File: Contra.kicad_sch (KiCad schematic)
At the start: 10 parts, among them J1 Conn_01x03, J2 Conn_01x02, SW1 SW_PUSH, SW2 SW_SPDT, U1 ProMicro

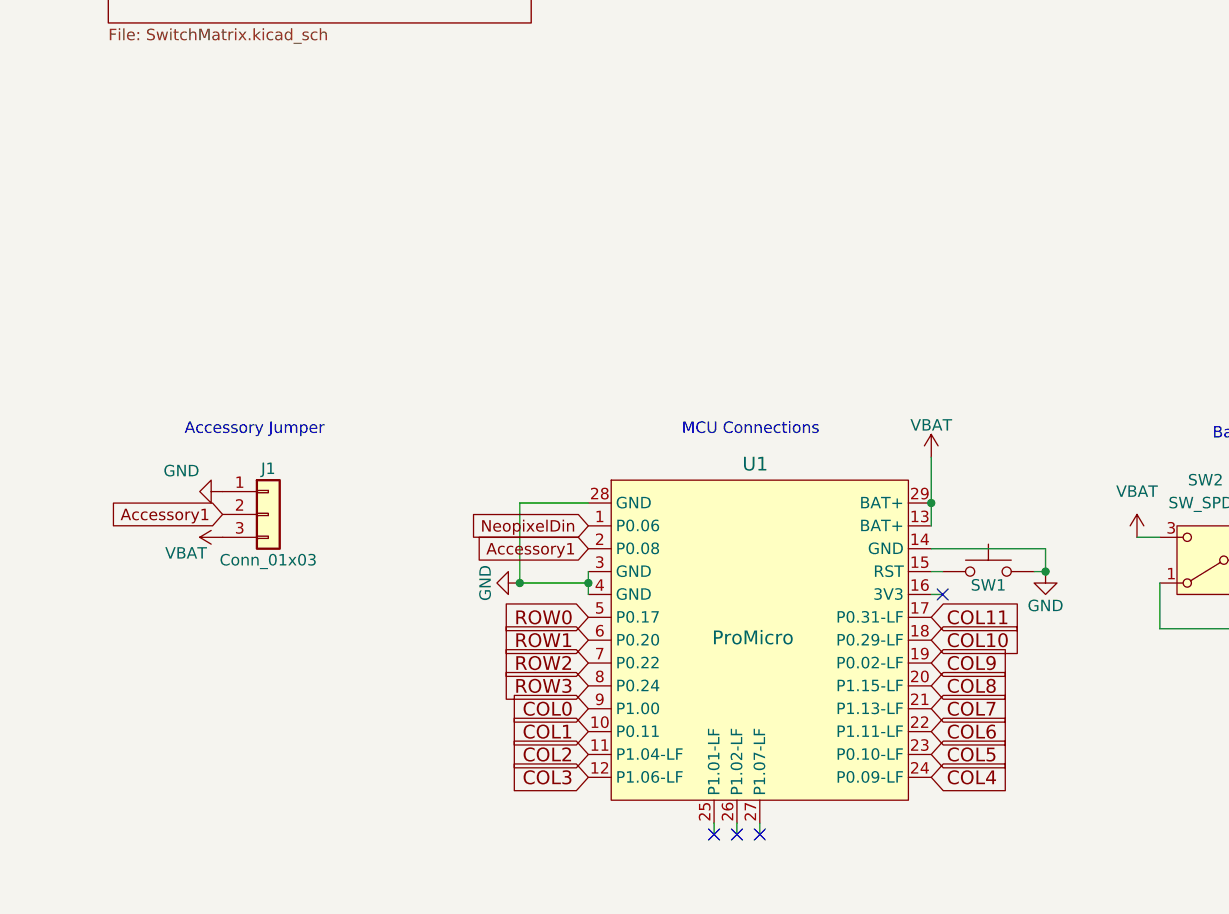
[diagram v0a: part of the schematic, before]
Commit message: add in OLED
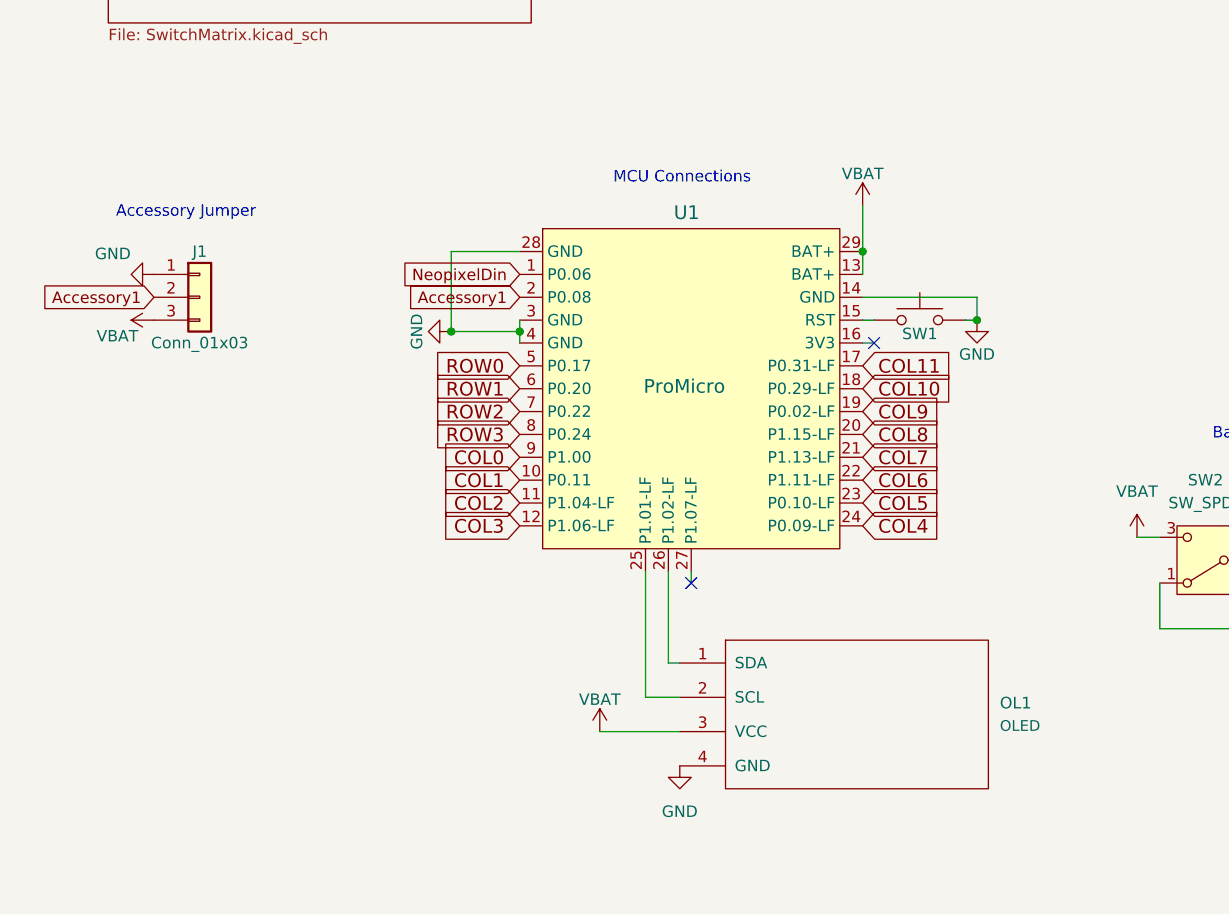
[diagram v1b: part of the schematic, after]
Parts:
- added OL1: OLED, kbd:OLED, symbol kbd:OLED
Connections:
- net GND: now also OL1.4 (GND)
- net VBAT: now also OL1.3 (VCC)
- net at U1.25 (P1.01-LF): now also OL1.2 (SCL)
- net at U1.26 (P1.02-LF): now also OL1.1 (SDA)
- no-connect marks 4 -> 2
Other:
- moved on the sheet: J1, SW1, U1

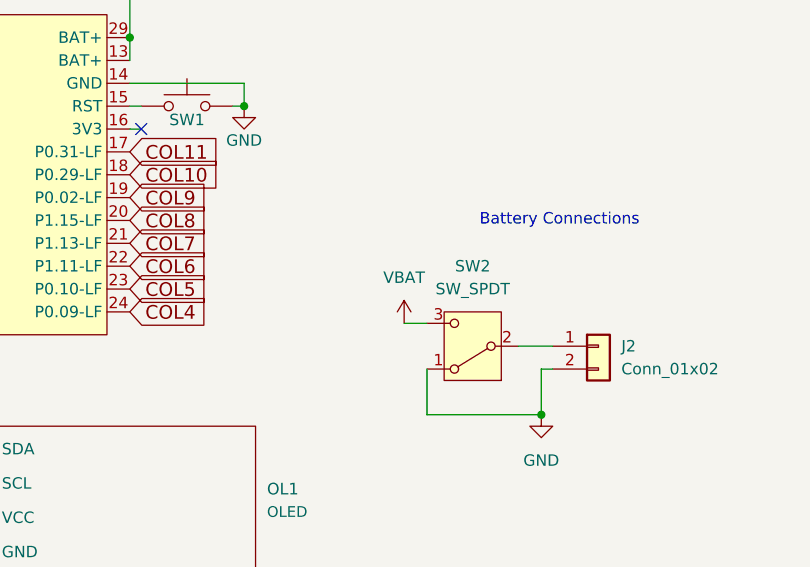
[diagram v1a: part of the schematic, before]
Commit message: change +5V to VBAT
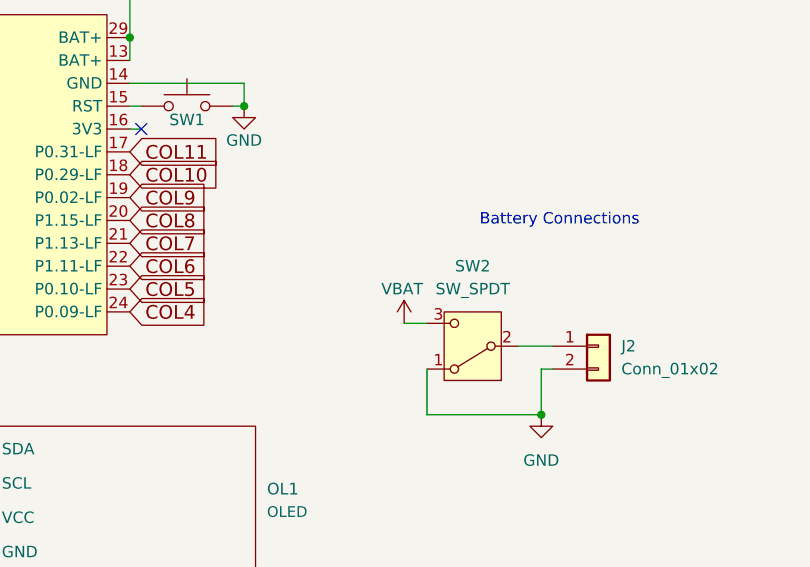
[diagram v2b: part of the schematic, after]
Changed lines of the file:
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@@
 		(in_pos_files yes)
 		(dnp no)
-		(fields_autoplaced yes)
 		(property "Reference" "#PWR03"
 			(at 142.24 158.75 0)
@@
 		)
 		(property "Value" "VBAT"
-			(at 142.24 149.86 0)
+			(at 139.7 151.13 0)
 			(show_name no)
 			(do_not_autoplace no)
@@
 					(size 1.27 1.27)
 				)
+				(justify left)
 			)
 		)

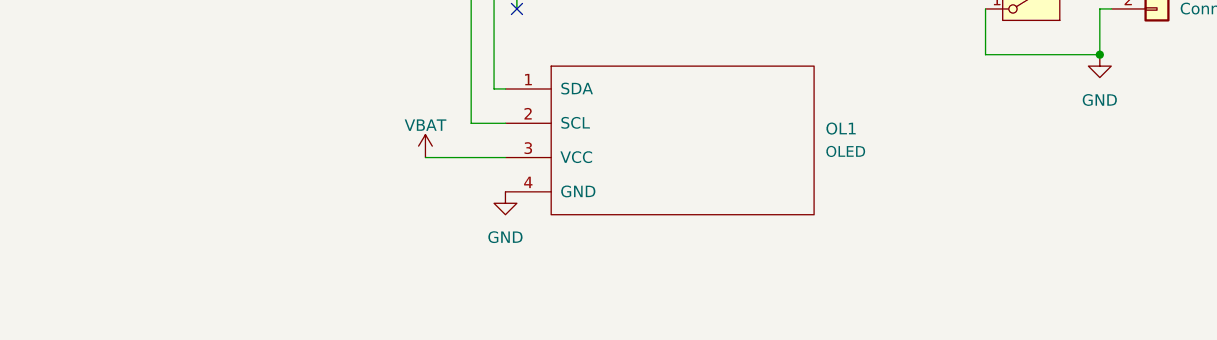
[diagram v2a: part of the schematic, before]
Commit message: add note about SDA and SCL
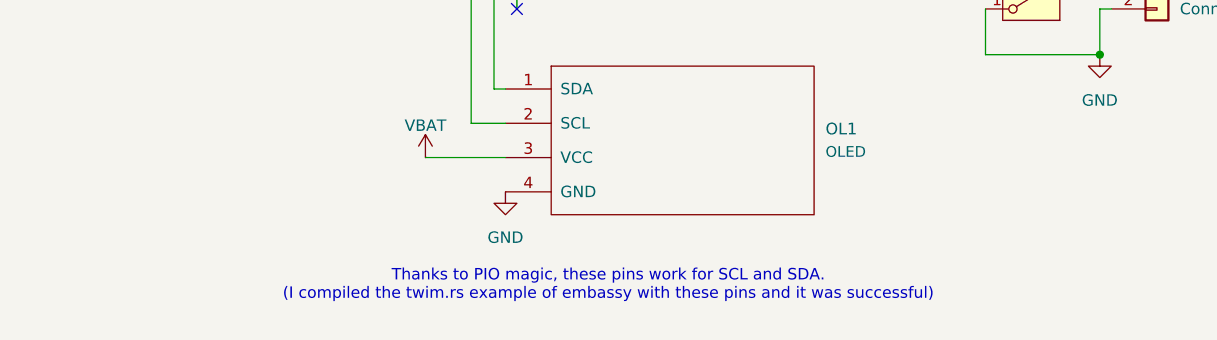
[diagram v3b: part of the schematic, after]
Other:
- note added: "Thanks to PIO magic, these pins work for SCL and SDA. (I compiled the twim.rs example of embassy with these pins and it was successful)"
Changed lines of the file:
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@@
+		)
+	)
+	(text "Thanks to PIO magic, these pins work for SCL and SDA. \n(I compiled the twim.rs example of embassy with these pins and it was successful)"
+		(exclude_from_sim no)
+		(at 102.87 190.754 0)
+		(effects
+			(font
+				(size 1.27 1.27)
+			)
 		)
 	)

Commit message: recover from crash. fix ground plane connection issue
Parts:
- H1: value MountingHole_Pad -> MountingHole; footprint MountingHole:MountingHole_2.2mm_M2_Pad -> MountingHole:MountingHole_2.2mm_M2; symbol Mechanical:MountingHole_Pad -> Mechanical:MountingHole
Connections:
- net GND: no longer H1.1
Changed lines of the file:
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@@
-	)
-	(junction
-		(at 168.91 36.83)
-		(diameter 0)
-		(color 0 0 0 0)
 	)
 	(junction
@@
 		(pts
 			(xy 111.76 123.19) (xy 111.76 125.73)
-		)
-		(stroke
-			(width 0)
-			(type default)
-		)
-	)
-	(wire
-		(pts
-			(xy 140.97 36.83) (xy 168.91 36.83)
 		)
 		(stroke
@@
 	)
 	(symbol
-		(lib_id "Mechanical:MountingHole_Pad")
+		(lib_id "Mechanical:MountingHole")
 		(at 140.97 34.29 0)
 		(unit 1)
@@
 		(fields_autoplaced yes)
 		(property "Reference" "H1"
-			(at 143.51 31.7499 0)
+			(at 143.51 33.0199 0)
 			(show_name no)
 			(do_not_autoplace no)
@@
 			)
 		)
-		(property "Value" "MountingHole_Pad"
-			(at 143.51 34.2899 0)
+		(property "Value" "MountingHole"
+			(at 143.51 35.5599 0)
 			(show_name no)
 			(do_not_autoplace no)
@@
 			)
 		)
-		(property "Footprint" "MountingHole:MountingHole_2.2mm_M2_Pad"
+		(property "Footprint" "MountingHole:MountingHole_2.2mm_M2"
 			(at 140.97 34.29 0)
 			(hide yes)
@@
 			)
 		)
-		(property "Description" "Mounting Hole with connection"
+		(property "Description" "Mounting Hole without connection"
 			(at 140.97 34.29 0)
 			(hide yes)
@@
 			)
 		)
-		(pin "1"
-		)
 		(instances
